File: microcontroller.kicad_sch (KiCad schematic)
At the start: 25 parts, among them J10 ESP_Only, J11 ESP32 [R], J12 SPI_EXPANSION, J13 I2C_EXPANSION, J16 ESP32 [L], J24 RPi Zero 2 W, J8 SHARED, J9 RPi_Only

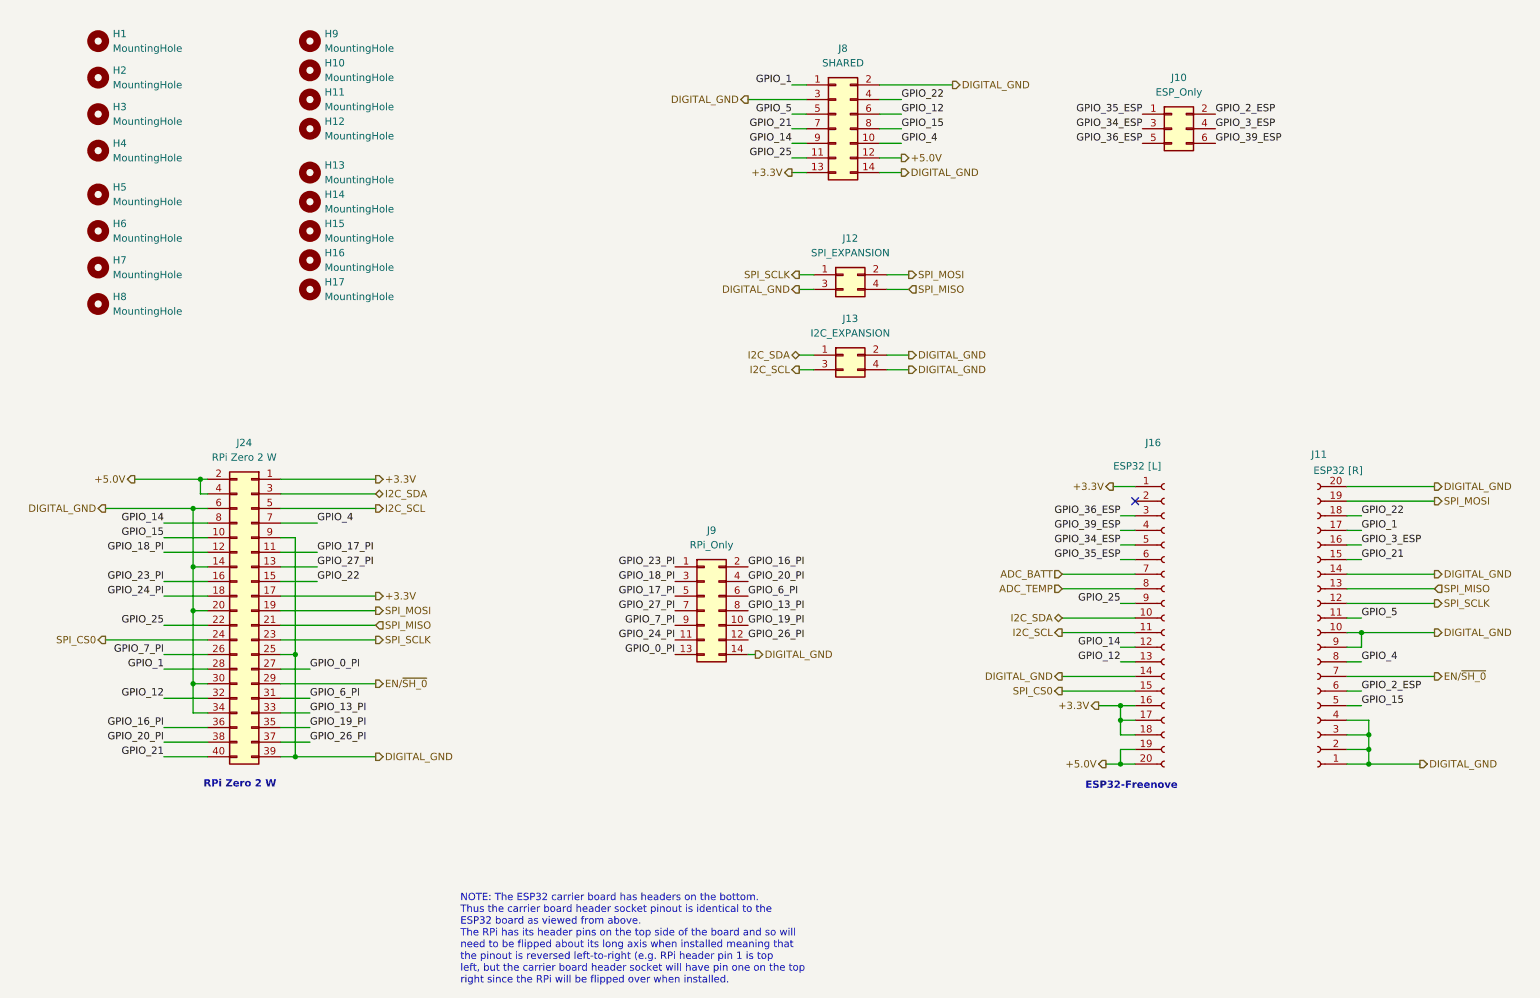
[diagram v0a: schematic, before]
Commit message: Prototype v0.3.1 WIP Just a maintenance checkin. Many changes - Removed the Base Sensor schematic and put all sensors into SensorPrototype - Added a constant current LED driver for camera illumination - Added a 12V buck converter to the input in support of external power - Added a low-side current sense to the input - Added an LDO regulator to cleanup Buck output and to provide battery regulation - Added support for an internal battery + switchover / charge circuit. - Swapped headers for proper board connectors - Added an RS485 transceiver for external + modem communication - Added an additional temperature circuit in support of NTC probes - Incorporated the AS Dissolved Oxygen sensor into the main board - Added DC return path resistors to non-inverting amps - Fixed mixed power domain bug - Moved AS isolated carrier board to 3.3V rail and routed the shutdown pin to en/sh - Moved the DHT20 to the 3.3V rail - In the process of re-routing ADC channels.
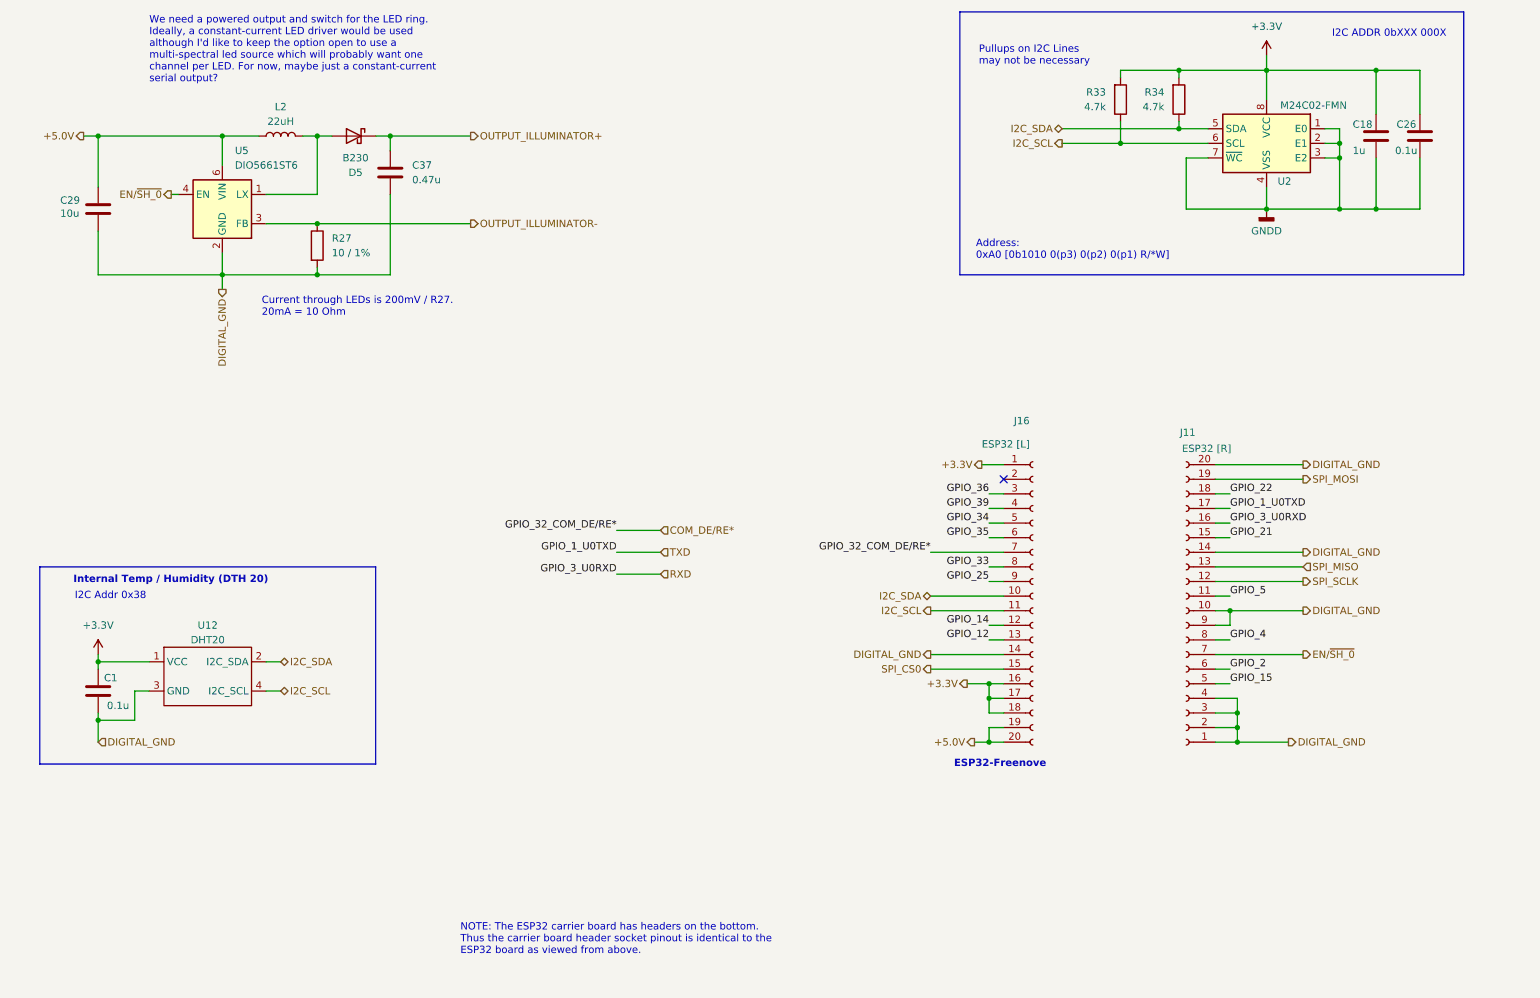
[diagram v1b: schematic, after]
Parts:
- removed H1, H10, H11, H12, H13, H14, H15, H16, H17, H2, H3, H4, H5, H6, H7, H8, H9: MountingHole, MountingHole:MountingHole_2.7mm_M2.5_ISO14580, symbol Mechanical:MountingHole
- removed J10: ESP_Only, Connector_PinHeader_2.54mm:PinHeader_2x03_P2.54mm_Vertical_SMD, symbol Connector_Generic:Conn_02x03_Odd_Even
- removed J12: SPI_EXPANSION, Connector_PinHeader_2.54mm:PinHeader_2x02_P2.54mm_Vertical_SMD, symbol Connector_Generic:Conn_02x02_Odd_Even
- removed J13: I2C_EXPANSION, Connector_PinHeader_2.54mm:PinHeader_2x02_P2.54mm_Vertical_SMD, symbol Connector_Generic:Conn_02x02_Odd_Even
- removed J24: RPi Zero 2 W, Connector_PinSocket_2.54mm:PinSocket_2x20_P2.54mm_Vertical_SMD, symbol Connector_Generic:Conn_02x20_Odd_Even
- removed J8: SHARED, Connector_PinHeader_2.54mm:PinHeader_2x07_P2.54mm_Vertical_SMD, symbol Connector_Generic:Conn_02x07_Odd_Even
- removed J9: RPi_Only, Connector_PinHeader_2.54mm:PinHeader_2x07_P2.54mm_Vertical_SMD, symbol Connector_Generic:Conn_02x07_Odd_Even
- added C1, C26: 0.1u, Capacitor_SMD:C_0805_2012Metric_Pad1.18x1.45mm_HandSolder, symbol Device:C
- added C18: 1u, Capacitor_SMD:C_0805_2012Metric_Pad1.18x1.45mm_HandSolder, symbol Device:C
- added C29: 10u, Capacitor_SMD:C_0805_2012Metric_Pad1.18x1.45mm_HandSolder, symbol Device:C
- added C37: 0.47u, Capacitor_SMD:C_0805_2012Metric_Pad1.18x1.45mm_HandSolder, symbol Device:C
- added D5: B230, Diode_SMD:D_SMB, symbol Diode:B230
- added L2: 22uH, Inductor_SMD:L_1210_3225Metric_Pad1.42x2.65mm_HandSolder, symbol Device:L
- added R27: 10 / 1%, symbol Device:R
- added R33, R34: 4.7k, Resistor_SMD:R_0805_2012Metric_Pad1.20x1.40mm_HandSolder, symbol Device:R
- added U12: DHT20, Connector_PinSocket_2.54mm:PinSocket_1x04_P2.54mm_Vertical_SMD_Pin1Left, symbol AndrewAdditions:DHT20
- added U2: M24C02-FMN, Package_SO:SOIC-8_3.9x4.9mm_P1.27mm, symbol Memory_EEPROM:M24C02-FMN
- added U5: DIO5661ST6, Package_TO_SOT_SMD:SOT-23-6, symbol Driver_LED:DIO5661ST6
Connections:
- net +3.3V: now also C1.1, C18.1, C26.1, R33.2, R34.2, U12.1 (VCC), U2.8 (VCC)
- net +5.0V: now also C29.1, L2.1, U5.6 (VIN)
- net DIGITAL_GND: now also C1.2, C29.2, C37.2, R27.2, U12.3 (GND), U5.2 (GND)
- net EN/~{SH_0}: now also U5.4 (EN)
- net I2C_SCL: now also R33.1, U12.4 (I2C_SCL), U2.6 (SCL)
- net I2C_SDA: now also R34.1, U12.2 (I2C_SDA), U2.5 (SDA)
- net ADC_BATT renamed COM_DE/RE*
- net ADC_TEMP renamed GPIO_33
- net GPIO_1 renamed TXD
- net GPIO_2_ESP renamed GPIO_2
- net GPIO_34_ESP renamed GPIO_34
- net GPIO_35_ESP renamed GPIO_35
- net GPIO_36_ESP renamed GPIO_36
- net GPIO_39_ESP renamed GPIO_39
- net GPIO_3_ESP renamed RXD
- new net: D5.2 (A), L2.2, U5.1 (LX)
- new net GNDD: C18.2, C26.2, U2.1 (E0), U2.2 (E1), U2.3 (E2), U2.4 (VSS), U2.7 (~{WC})
- new net OUTPUT_ILLUMINATOR+: C37.1, D5.1 (K)
- new net OUTPUT_ILLUMINATOR-: R27.1, U5.3 (FB)
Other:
- note added: "Address: 0xA0 [0b1010 0(p3) 0(p2) 0(p1) R/*W]"
- note added: "Current through LEDs is 200mV / R27. 20mA = 10 Ohm"
- note added: "I2C ADDR 0bXXX 000X"
- note added: "I2C Addr 0x38"
- note added: "Internal Temp / Humidity (DTH 20)"
- note added: "NOTE: The ESP32 carrier board has headers on the bottom. Thus the carrier board header socket pinout is identical to the ESP32 board as viewed from above."
- note added: "Pullups on I2C Lines may not be necessary"
- note added: "We need a powered output and switch for the LED ring. Ideally, a constant-current LED driver would be used although I'd like to keep the option open to use a multi-spectral led source which will probably want one channel per LED. For now, maybe just a constant-current serial output?"
- note removed: "NOTE: The ESP32 carrier board has headers on the bottom. Thus the carrier board header socket pinout is identical to the ESP32 board as viewed from above. The RPi has its header pins on the top side of the board and so will need to be flipped about its long axis when installed meaning that the pinout is reversed left-to-right (e.g. RPi header pin 1 is top left, but the carrier board header socket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"
- note removed: "RPi Zero 2 W"
- moved on the sheet: J11, J16

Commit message: Board V0.0.3 Everything is routed and connected ERC and DRC run without serious error. (There are DRC violations due to a VSSP-83x3mm package but I'm not sure why)
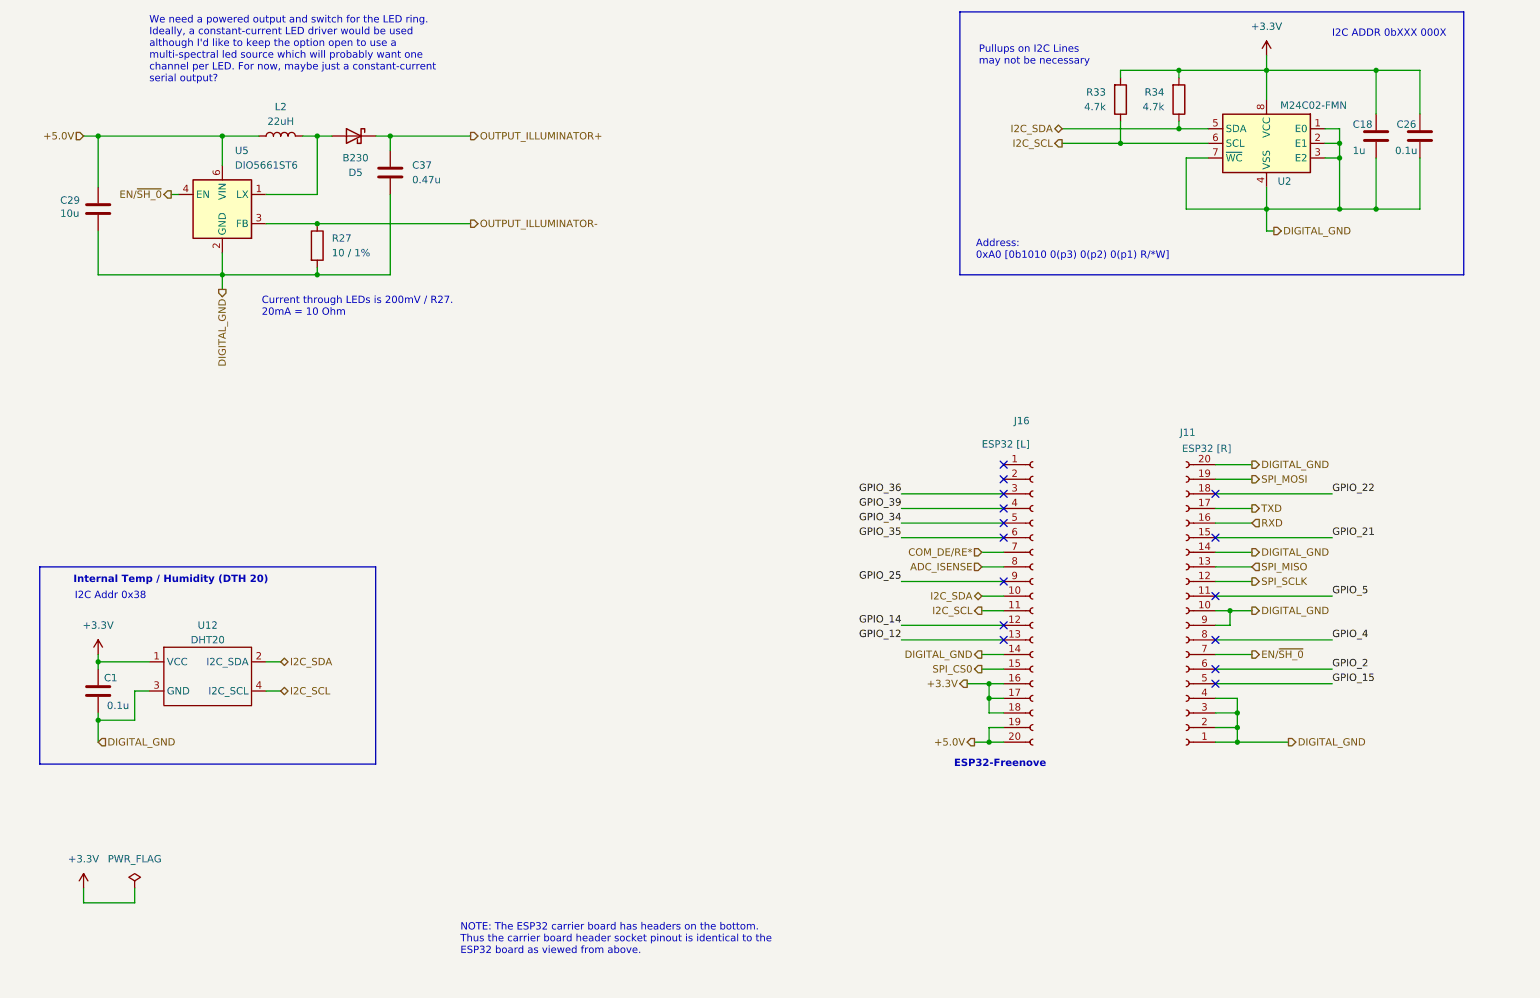
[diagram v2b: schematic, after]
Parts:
- R27: footprint (none) -> Resistor_SMD:R_0805_2012Metric_Pad1.20x1.40mm_HandSolder
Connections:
- net GNDD is gone; now on net DIGITAL_GND: C18.2, C26.2, U2.1 (E0), U2.2 (E1), U2.3 (E2), U2.4 (VSS), U2.7 (~{WC})
- net +3.3V: no longer J16.1 (Pin_1)
- net GPIO_33 renamed ADC_ISENSE
- no-connect marks 1 -> 15

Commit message: feature/v3.1/setup - Inception - some general changes in support of v3.1 before I thought to branch.
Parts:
- C1, C26: MPN (none) -> CC0805KRX7R7BB104; Manufacturer (none) -> YAGEO; Package (none) -> 0805
- C18: MPN (none) -> CL21B105KOFNNNG; Manufacturer (none) -> Samsung; Package (none) -> 0805
- C29: MPN (none) -> CL21B106KPQNNNE; Manufacturer (none) -> Samsung; Package (none) -> 0805
- C37: MPN (none) -> CL21B474KOFNNNE; Manufacturer (none) -> Samsung; Package (none) -> 0805
- D5: MPN (none) -> B230-13-F; Manufacturer (none) -> Diodes Inc.; Package (none) -> SMB
- J11, J16, U12: now not fitted
- L2: MPN (none) -> CBC3225T220KR; Manufacturer (none) -> Tayo Yuden; Package (none) -> 1210
- R27: MPN (none) -> AC0805FR-7W10RL; Manufacturer (none) -> YAGEO; Package (none) -> 0805
- R33, R34: value 4.7k -> 3.3k; MPN (none) -> AC0805FR-7W4K7L; Manufacturer (none) -> YAGEO; Package (none) -> 0805
- U2: MPN (none) -> M24C02-FMN; Manufacturer (none) -> ST; Package (none) -> SOIC-8
- U5: MPN (none) -> DIO5661ST6; Manufacturer (none) -> DIOO; Package (none) -> SOT-23-6
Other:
- note added: "BUG: Audit the strapping pins. When attached to the board, the ESP32 module boots in a protected mode. This may be due to the strapping pins being held low. Possibly GPIO_0 is the culprit. Add a pullup or pulldown where appropriate on these pins for proper booting."
